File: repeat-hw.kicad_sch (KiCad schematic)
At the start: 0 parts

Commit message: added W5100
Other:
- added sheet Ethernet (W5100.kicad_sch)

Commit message: Finishe PoE and ethernet
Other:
- sheet Ethernet renamed W5100 + PoE
- sheet W5100 + PoE ports: added 5V, CLK, MISO, MOSI, ~{CS}, ~{INT}, ~{RST}; removed none

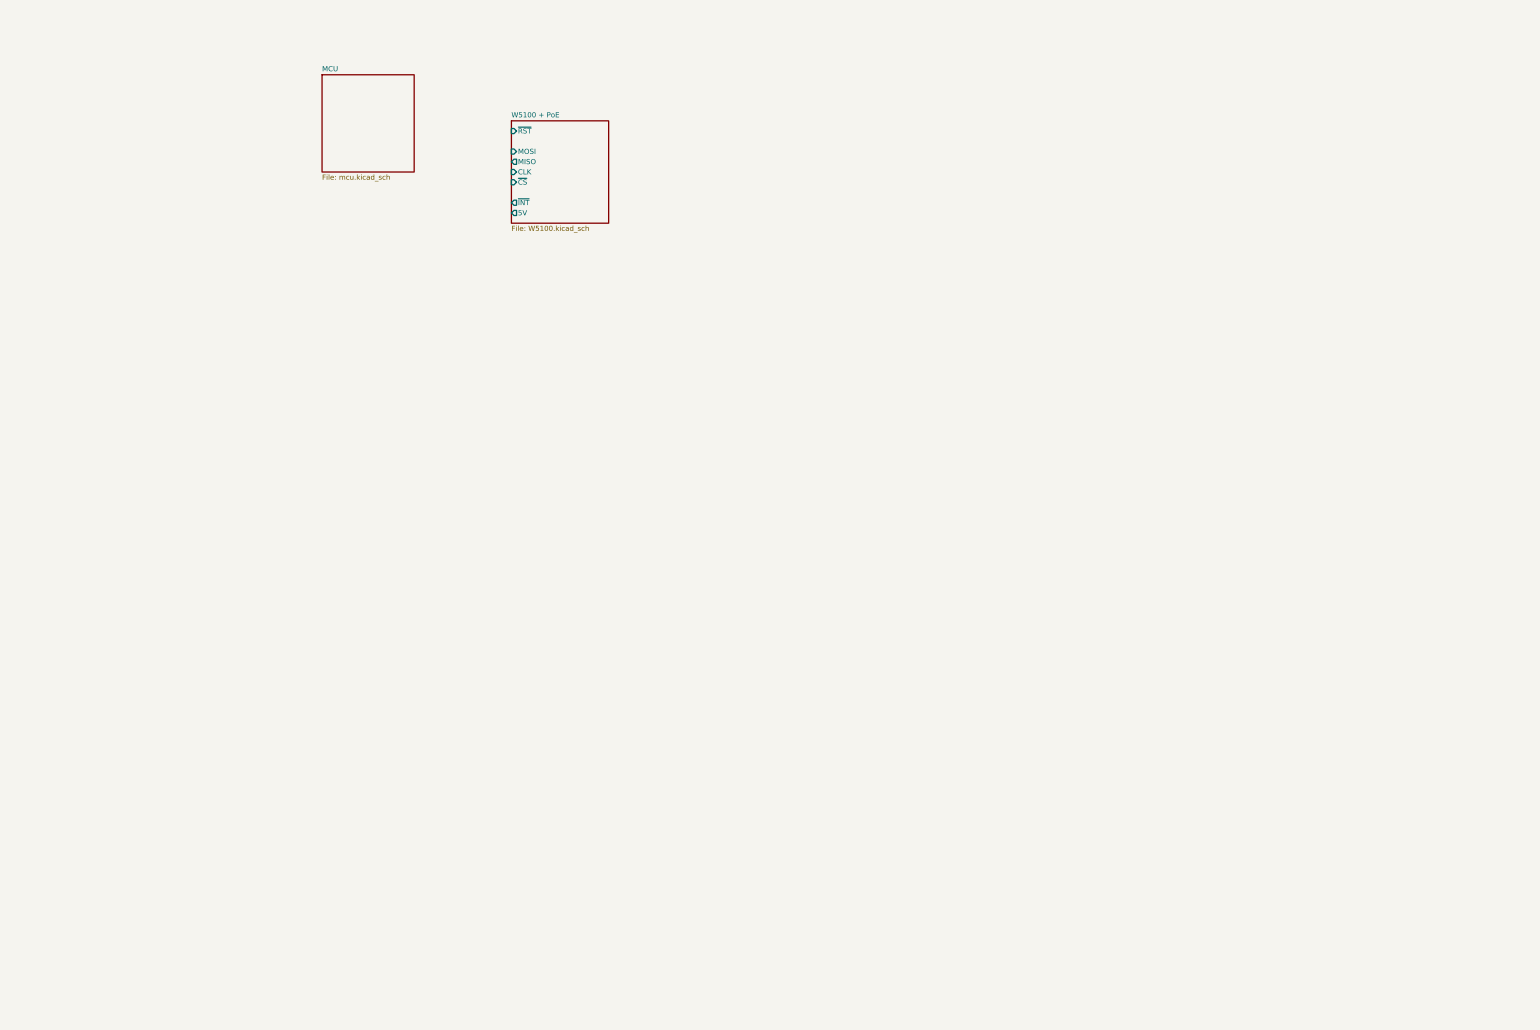
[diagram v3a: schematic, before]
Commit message: Added USB port
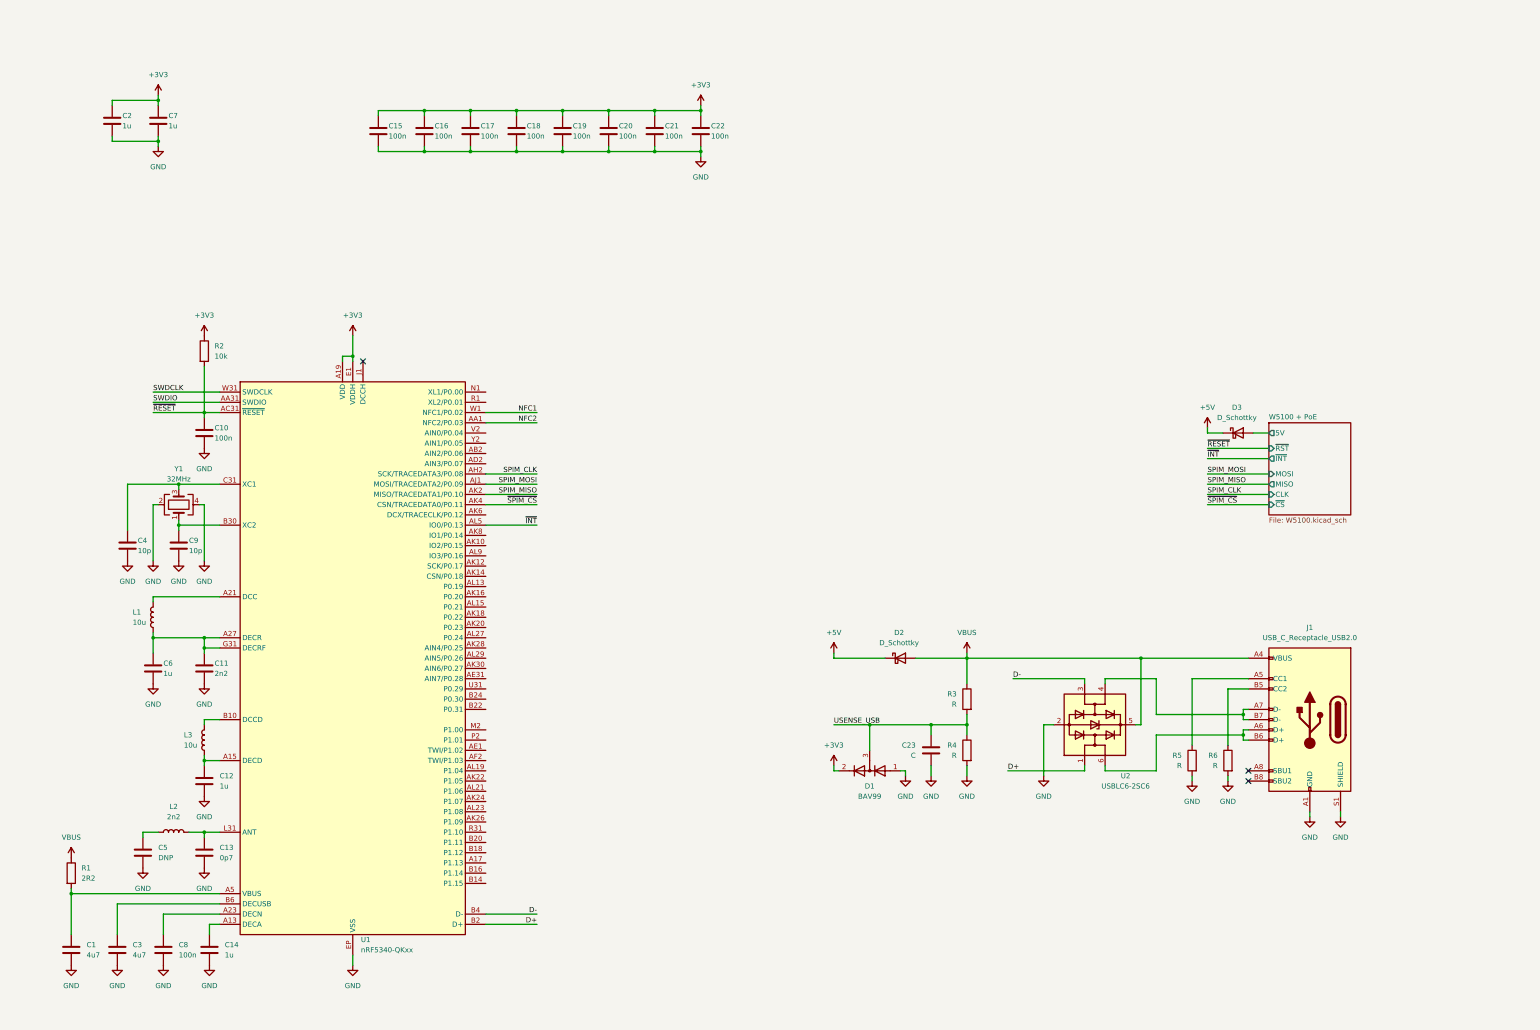
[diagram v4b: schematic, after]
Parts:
- added C1: 4u7, Connector_RJ:RJ45_Cetus_J1B1211CCD_Horizontal, symbol Device:C
- added C10, C15, C16, C17, C18, C19, C20, C21, C22, C8: 100n, Capacitor_SMD:C_0402_1005Metric, symbol Device:C
- added C11: 2n2, Capacitor_SMD:C_0402_1005Metric, symbol Device:C
- added C12, C14, C6, C7: 1u, symbol Device:C
- added C13: 0p7, Capacitor_SMD:C_0402_1005Metric, symbol Device:C
- added C2: 1u, Capacitor_SMD:C_0402_1005Metric, symbol Device:C
- added C23: C, symbol Device:C
- added C3: 4u7, symbol Device:C
- added C4, C9: 10p, Capacitor_SMD:C_0402_1005Metric, symbol Device:C
- added C5: DNP, symbol Device:C
- added D1: BAV99, Package_TO_SOT_SMD:SOT-23, symbol Diode:BAV99
- added D2, D3: D_Schottky, symbol Device:D_Schottky
- added J1: USB_C_Receptacle_USB2.0, Connector_USB:USB_C_Receptacle_XKB_U262-16XN-4BVC11, symbol Connector:USB_C_Receptacle_USB2.0
- added L1, L3: 10u, symbol Device:L
- added L2: 2n2, Capacitor_SMD:C_0402_1005Metric, symbol Device:L
- added R1: 2R2, Resistor_SMD:R_0402_1005Metric, symbol Device:R
- added R2: 10k, Resistor_SMD:R_0402_1005Metric, symbol Device:R
- added R3, R4, R5, R6: R, Resistor_SMD:R_0402_1005Metric, symbol Device:R
- added U1: nRF5340-QKxx, Package_DFN_QFN:Nordic_AQFN-94-1EP_7x7mm_P0.4mm, symbol MCU_Nordic:nRF5340-QKxx
- added U2: USBLC6-2SC6, Package_TO_SOT_SMD:SOT-23-6, symbol Power_Protection:USBLC6-2SC6
- added Y1: 32MHz, Crystal:Crystal_SMD_3225-4Pin_3.2x2.5mm, symbol Device:Crystal_GND24
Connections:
- net W5100 + PoE/5V: now also D3.2 (A)
- new net: J1.B5 (CC2), R6.1
- new net: C11.1, C6.1, L1.1, U1.A27 (DECR), U1.G31 (DECRF)
- new net: J1.A5 (CC1), R5.1
- new net: J1.A6 (D+), J1.B6 (D+), U2.6 (I/O1)
- new net: J1.A7 (D-), J1.B7 (D-), U2.4 (I/O2)
- new net: C5.1, L2.1
- new net: C13.1, L2.2, U1.L31 (ANT)
- new net: C4.1, U1.C31 (XC1), Y1.3
- new net: C3.1, U1.B6 (DECUSB)
- new net: C9.1, U1.B30 (XC2), Y1.1
- new net: C8.1, U1.A23 (DECN)
- new net: C1.1, R1.2, U1.A5 (VBUS)
- new net: C12.1, L3.1, U1.A15 (DECD)
- new net: L3.2, U1.B10 (DCCD)
- new net: C14.1, U1.A13 (DECA)
- new net: L1.2, U1.A21 (DCC)
- new net +3V3: C15.1, C16.1, C17.1, C18.1, C19.1, C2.1, C20.1, C21.1, C22.1, C7.1, D1.2 (A), R2.1, U1.A19 (VDD), U1.AC1 (VDD), U1.AG1 (VDD), U1.AJ31 (VDD), U1.AL11 (VDD), U1.AL17 (VDD), U1.AL25 (VDD), U1.AL3 (VDD), U1.AL7 (VDD), U1.B28 (VDD), U1.B8 (VDD), U1.C1 (VDD), U1.E1 (VDDH), U1.E31 (VDD), U1.L1 (VDD), U1.N31 (VDD), U1.U1 (VDD)
- new net +5V: D2.1 (K), D3.1 (K)
- new net D+: U1.B2 (D+), U2.1 (I/O1)
- new net D-: U1.B4 (D-), U2.3 (I/O2)
- new net GND: C1.2, C10.2, C11.2, C12.2, C13.2, C14.2, C15.2, C16.2, C17.2, C18.2, C19.2, C2.2, C20.2, C21.2, C22.2, C23.2, C3.2, C4.2, C5.2, C6.2, C7.2, C8.2, C9.2, D1.1 (K), J1.A1 (GND), J1.A12 (GND), J1.B1 (GND), J1.B12 (GND), J1.S1 (SHIELD), R4.2, R5.2, R6.2, U1.EP (VSS), U2.2 (GND), Y1.2, Y1.4
- new net NFC1: U1.W1 (NFC1/P0.02)
- new net NFC2: U1.AA1 (NFC2/P0.03)
- new net SPIM_CLK: U1.AH2 (SCK/TRACEDATA3/P0.08)
- new net SPIM_MISO: U1.AK2 (MISO/TRACEDATA1/P0.10)
- new net SPIM_MOSI: U1.AJ1 (MOSI/TRACEDATA2/P0.09)
- new net SWDCLK: U1.W31 (SWDCLK)
- new net SWDIO: U1.AA31 (SWDIO)
- new net USENSE_USB: C23.1, D1.3 (K), R3.2, R4.1
- new net VBUS: D2.2 (A), J1.A4 (VBUS), J1.A9 (VBUS), J1.B4 (VBUS), J1.B9 (VBUS), R1.1, R3.1, U2.5 (VBUS)
- new net ~{INT}: U1.AL5 (IO0/P0.13)
- new net ~{RESET}: C10.1, R2.2, U1.AC31 (~{RESET})
- new net ~{SPIM_CS}: U1.AK4 (CSN/TRACEDATA0/P0.11)
- no-connect marks 0 -> 3
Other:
- removed sheet MCU

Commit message: Polished schematic
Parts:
- removed D2, D3: D_Schottky, symbol Device:D_Schottky
- added AE1: SWRA117D, RF_Antenna:Texas_SWRA117D_2.4GHz_Left, symbol Device:Antenna_Dipole
- added AE2: NFC, symbol Device:Antenna_Loop
- added C57: 10u, Capacitor_SMD:C_0603_1608Metric, symbol Device:C
- added C58: 47u, symbol Device:C_Polarized
- added C62, C63, C68: 1p, Capacitor_SMD:C_0402_1005Metric, symbol Device:C
- added C64, C65: 2p, Capacitor_SMD:C_0402_1005Metric, symbol Device:C
- added C66: 100n, Capacitor_SMD:C_0402_1005Metric, symbol Device:C
- added C67: 10u, Capacitor_SMD:C_0402_1005Metric, symbol Device:C
- added C70, C71, C72: 1u, Capacitor_SMD:C_0603_1608Metric, symbol Device:C
- added C77, C78, C79, C80: TBD, symbol Device:C
- added D2, D3: PMEG3010EJ, Diode_SMD:D_SOD-323F, symbol Diode:PMEG3010EJ
- added D4: BAV99, Package_TO_SOT_SMD:SOT-23, symbol Diode:BAV99
- added J3: Conn_Coaxial, Connector_Coaxial:U.FL_Hirose_U.FL-R-SMT-1_Vertical, symbol Connector:Conn_Coaxial
- added L5, L6: 3n, Capacitor_SMD:C_0402_1005Metric, symbol Device:L
- added L7, L8: 1n9, Capacitor_SMD:C_0402_1005Metric, symbol Device:L
- added R21: 180k, Resistor_SMD:R_0402_1005Metric, symbol Device:R
- added R8: 100k, Resistor_SMD:R_0402_1005Metric, symbol Device:R
- added U7: nRF21540, Package_DFN_QFN:QFN-16-1EP_4x4mm_P0.65mm_EP2.7x2.7mm_ThermalVias, symbol nordic:nRF21540
- added U9: AMS1117-3.3, Package_TO_SOT_SMD:SOT-223-3_TabPin2, symbol Regulator_Linear:AMS1117-3.3
- C1: footprint Connector_RJ:RJ45_Cetus_J1B1211CCD_Horizontal -> Capacitor_SMD:C_0603_1608Metric
- C12, C14, C3, C6: footprint (none) -> Capacitor_SMD:C_0603_1608Metric
- C2: value 1u -> 100n
- C23: value C -> 100n; footprint (none) -> Capacitor_SMD:C_0402_1005Metric
- C5: footprint (none) -> Capacitor_SMD:C_0402_1005Metric
- C7: value 1u -> 100n; footprint (none) -> Capacitor_SMD:C_0402_1005Metric
- R3: value R -> 100k
- R4: value R -> 180k
- R5, R6: value R -> 5k1
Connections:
- net +3V3: now also C58.1, C66.1, C67.1, C70.1, C71.1, C72.1, D4.2 (A), U7.5 (VDD), U7.6 (VDD), U9.2 (VO); no longer C2.1, C7.1
- net +5V: now also C7.1, C57.1, D2.1 (K), D3.1 (K), U9.3 (VI)
- net D+: now also J1.A6 (D+), J1.B6 (D+), U2.6 (I/O1); no longer U1.B2 (D+), U2.1 (I/O1)
- net D-: now also J1.A7 (D-), J1.B7 (D-), U2.4 (I/O2); no longer U1.B4 (D-), U2.3 (I/O2)
- net GND: now also AE1.1, C57.2, C58.2, C62.2, C63.2, C64.2, C65.2, C66.2, C67.2, C70.2, C71.2, C72.2, C77.1, C78.2, C79.1, C80.2, D4.1 (K), J3.2 (Ext), R21.2, U7.1 (GND), U7.16 (GND), U7.17 (GND), U9.1 (GND)
- net NFC1: now also AE2.1, C77.2, C79.2
- net NFC2: now also AE2.2, C78.1, C80.1
- net VBUS: now also D3.2 (A)
- net W5100 + PoE/5V: now also D2.2 (A), R8.1
- net at C5.1, L2.1: now also C68.2
- new net: C68.1, U7.10 (TRX)
- new net: L7.2, U7.2 (ANT1)
- new net: L8.2, U7.3 (ANT2)
- new net: AE1.2, C62.1, L5.1
- new net: C63.1, J3.1 (In), L6.1
- new net: C64.1, L5.2, L7.1
- new net: C65.1, L6.2, L8.1
- new net ESD_D+: U1.B2 (D+), U2.1 (I/O1)
- new net ESD_D-: U1.B4 (D-), U2.3 (I/O2)
- new net USENSE_POE: C2.1, D4.3 (K), R21.1, R8.2
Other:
- sheet W5100 + PoE: file W5100.kicad_sch -> W5100_PoE.kicad_sch
- sheet W5100 + PoE ports: added PLOSS; removed none
- moved on the sheet: C1, C10, C11, C12, C13, C14, C15, C16, C17, C18, C19, C20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

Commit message: Hopefully finished schematic
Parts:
- added C?: 100n, Capacitor_SMD:C_0402_1005Metric, symbol Device:C
- added U?: MX25R3235FZNxx0, Package_SON:WSON-8-1EP_6x5mm_P1.27mm_EP3.4x4mm, symbol Memory_Flash:MX25R3235FZNxx0
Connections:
- net +3V3: now also C?.1, U?.8 (VCC)
- net GND: now also C?.2, U?.4 (GND), U?.9 (GND)
- net SPIM_CLK: now also U7.12 (SCK)
- net SPIM_MISO: now also U7.14 (MISO)
- net SPIM_MOSI: now also U7.13 (MOSI)
- net USENSE_POE: now also U1.Y2 (AIN1/P0.05)
- net USENSE_USB: now also U1.V2 (AIN0/P0.04)
- net ~{FEM_PDN}: now reaches U7.11 (~{PDN})
- net ~{FEM_PDN}: now also U1.AL29 (AIN5/P0.26)
- net ~{FEM_CS}: now reaches U7.15 (~{CSN})
- net ~{FEM_CS}: now also U1.AL15 (P0.21)
- net FEM_MODE: now reaches U7.4 (MODE)
- net FEM_MODE: now also U1.AK18 (P0.22)
- net FEM_RXEN: now reaches U7.7 (RXEN)
- net FEM_RXEN: now also U1.AK20 (P0.23)
- net FEM_ANTSEL: now reaches U7.8 (ANTSEL)
- net FEM_ANTSEL: now also U1.AK28 (AIN4/P0.25)
- net FEM_TXEN: now reaches U7.9 (TXEN)
- net FEM_TXEN: now also U1.AL27 (P0.24)
- net QSPI2: now reaches U1.AK10 (IO2/P0.15)
- net QSPI2: now also U?.3 (~{WP}/SIO2)
- net QSPI_CLK: now reaches U1.AK12 (SCK/P0.17)
- net QSPI_CLK: now also U?.6 (SCLK)
- net ~{QSPI_CS}: now reaches U1.AK14 (CSN/P0.18)
- net ~{QSPI_CS}: now also U?.1 (~{CS})
- net ~{ETH_RST}: now reaches U1.AK16 (P0.20)
- net QSPI1: now reaches U1.AK8 (IO1/P0.14)
- net QSPI1: now also U?.2 (SO/SIO1)
- net ~{ETH_INT}: now reaches U1.AL13 (P0.19)
- net QSPI3: now reaches U1.AL9 (IO3/P0.16)
- net QSPI3: now also U?.7 (~{RESET}/SIO3)
- net ~{INT} renamed QSPI0
- net QSPI0: now also U?.5 (SI/SIO0)
- net ~{SPIM_CS} renamed ~{ETH_CS}
- no-connect marks 3 -> 29
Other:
- moved on the sheet: C15, C16, C17, C18, C19, C20, C21, C22, C68, C71, C72

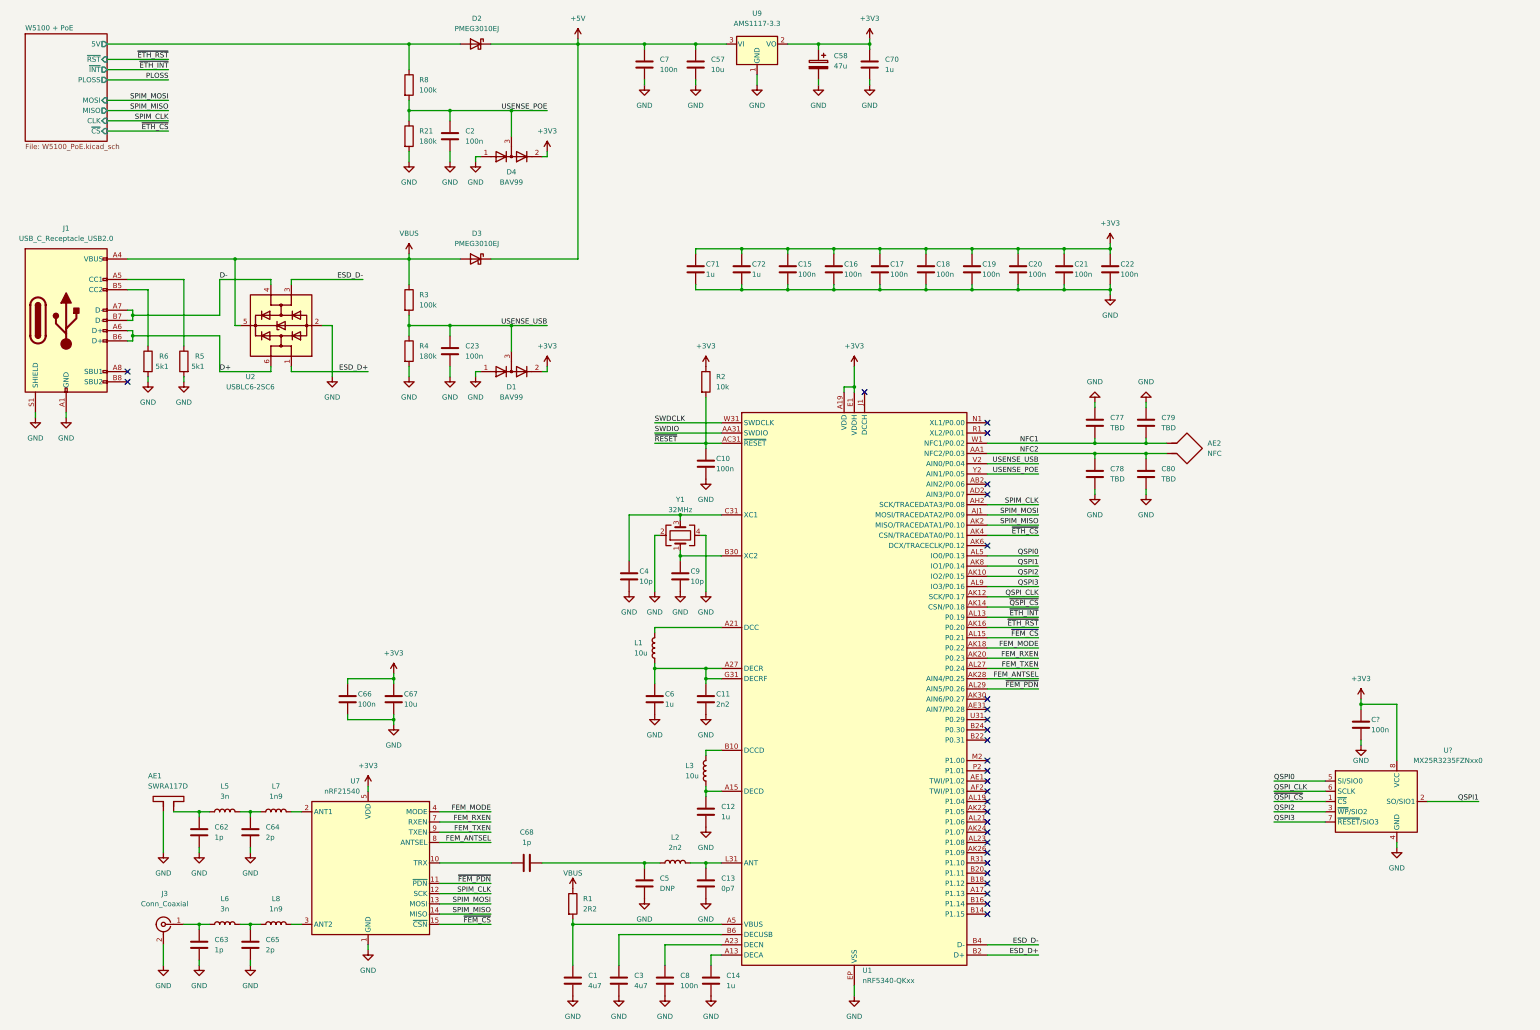
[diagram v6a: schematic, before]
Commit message: Routing half done
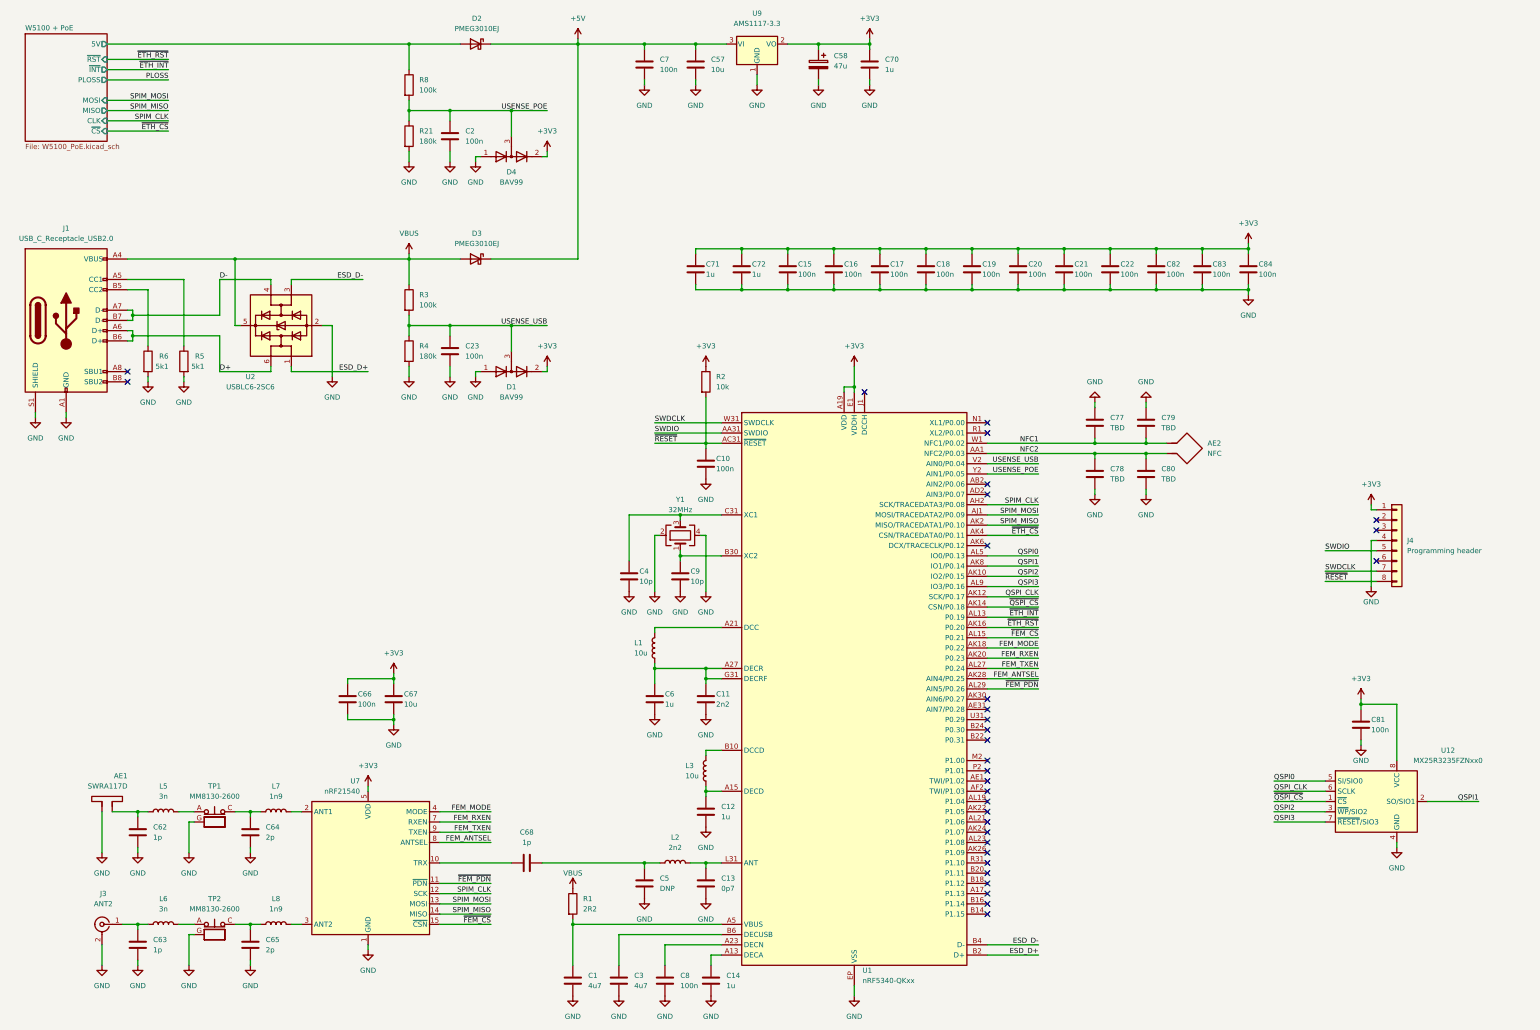
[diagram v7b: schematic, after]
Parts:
- added C82, C83, C84: 100n, Capacitor_SMD:C_0402_1005Metric, symbol Device:C
- added J4: Programming header, soicbite:SOIC_clipProgSmall, symbol Connector_Generic:Conn_01x08
- added TP1, TP2: MM8130-2600, murrata:MM8130-2600, symbol Connector:CoaxialSwitch_Testpoint
- C58: footprint (none) -> Capacitor_Tantalum_SMD:CP_EIA-2012-12_Kemet-R
- C77, C78, C79, C80: footprint (none) -> Capacitor_SMD:C_0402_1005Metric
- J3: value Conn_Coaxial -> ANT2
- L1, L3: footprint (none) -> Inductor_SMD:L_0603_1608Metric
- gave numbers to parts that had none: 2
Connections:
- net +3V3: now also C82.1, C83.1, C84.1, J4.1 (Pin_1)
- net GND: now also AE1.2, C82.2, C83.2, C84.2, J4.4 (Pin_4), TP1.G, TP2.G; no longer AE1.1
- net SWDCLK: now also J4.7 (Pin_7)
- net SWDIO: now also J4.5 (Pin_5)
- net ~{RESET}: now also J4.8 (Pin_8)
- net at C62.1, L5.1: now also AE1.1; no longer AE1.2
- net at C64.1, L7.1: now also TP1.C; no longer L5.2
- net at C65.1, L8.1: now also TP2.C; no longer L6.2
- new net: L6.2, TP2.A
- new net: L5.2, TP1.A
- no-connect marks 29 -> 32
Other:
- moved on the sheet: AE1, C62, C63, J3, L5, L6
